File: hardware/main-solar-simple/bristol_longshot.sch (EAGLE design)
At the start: 65 parts, among them U1 SAM_D20E, U2 SI4060, U3 UBLOX_MAX, U4 SST25WF040BT-40I/NP, U5 TG-5006CJ, U6 LTC3105EDDPBF, U7 TPS3123, U8 SN74LVC1G32DCKR, U9 BMP180

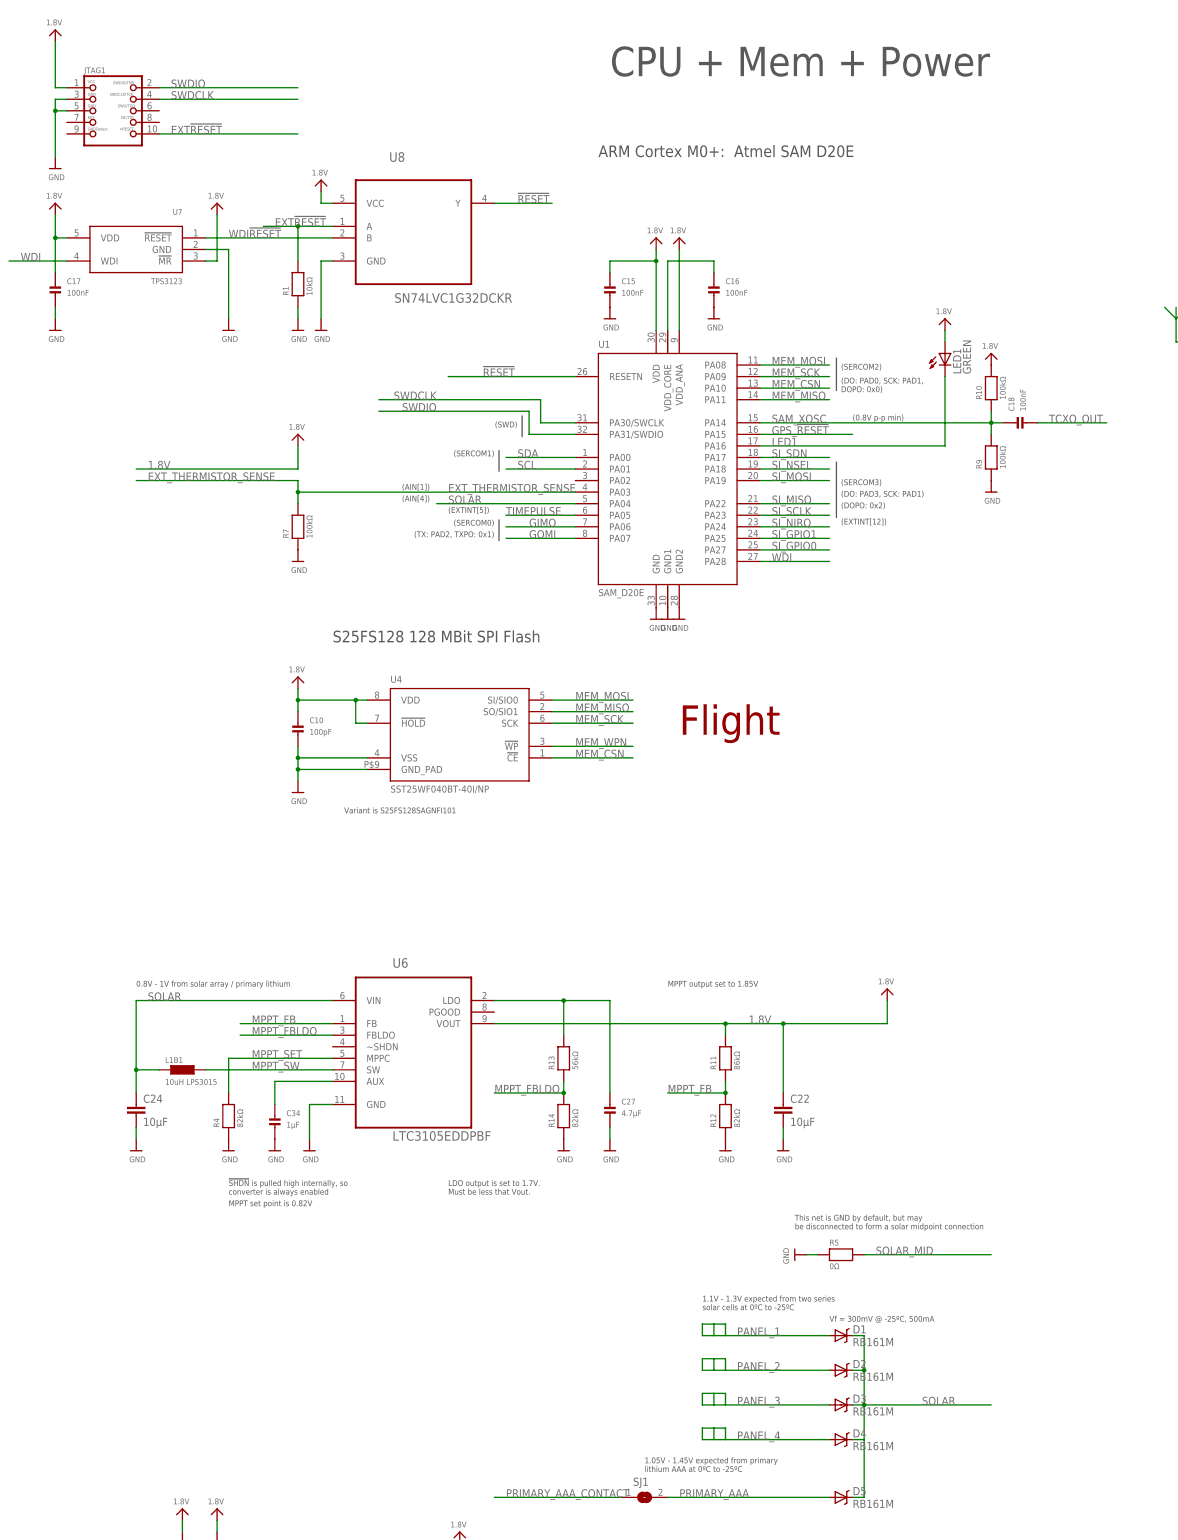
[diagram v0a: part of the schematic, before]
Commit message: Updated schematic labels, fixed R11 value
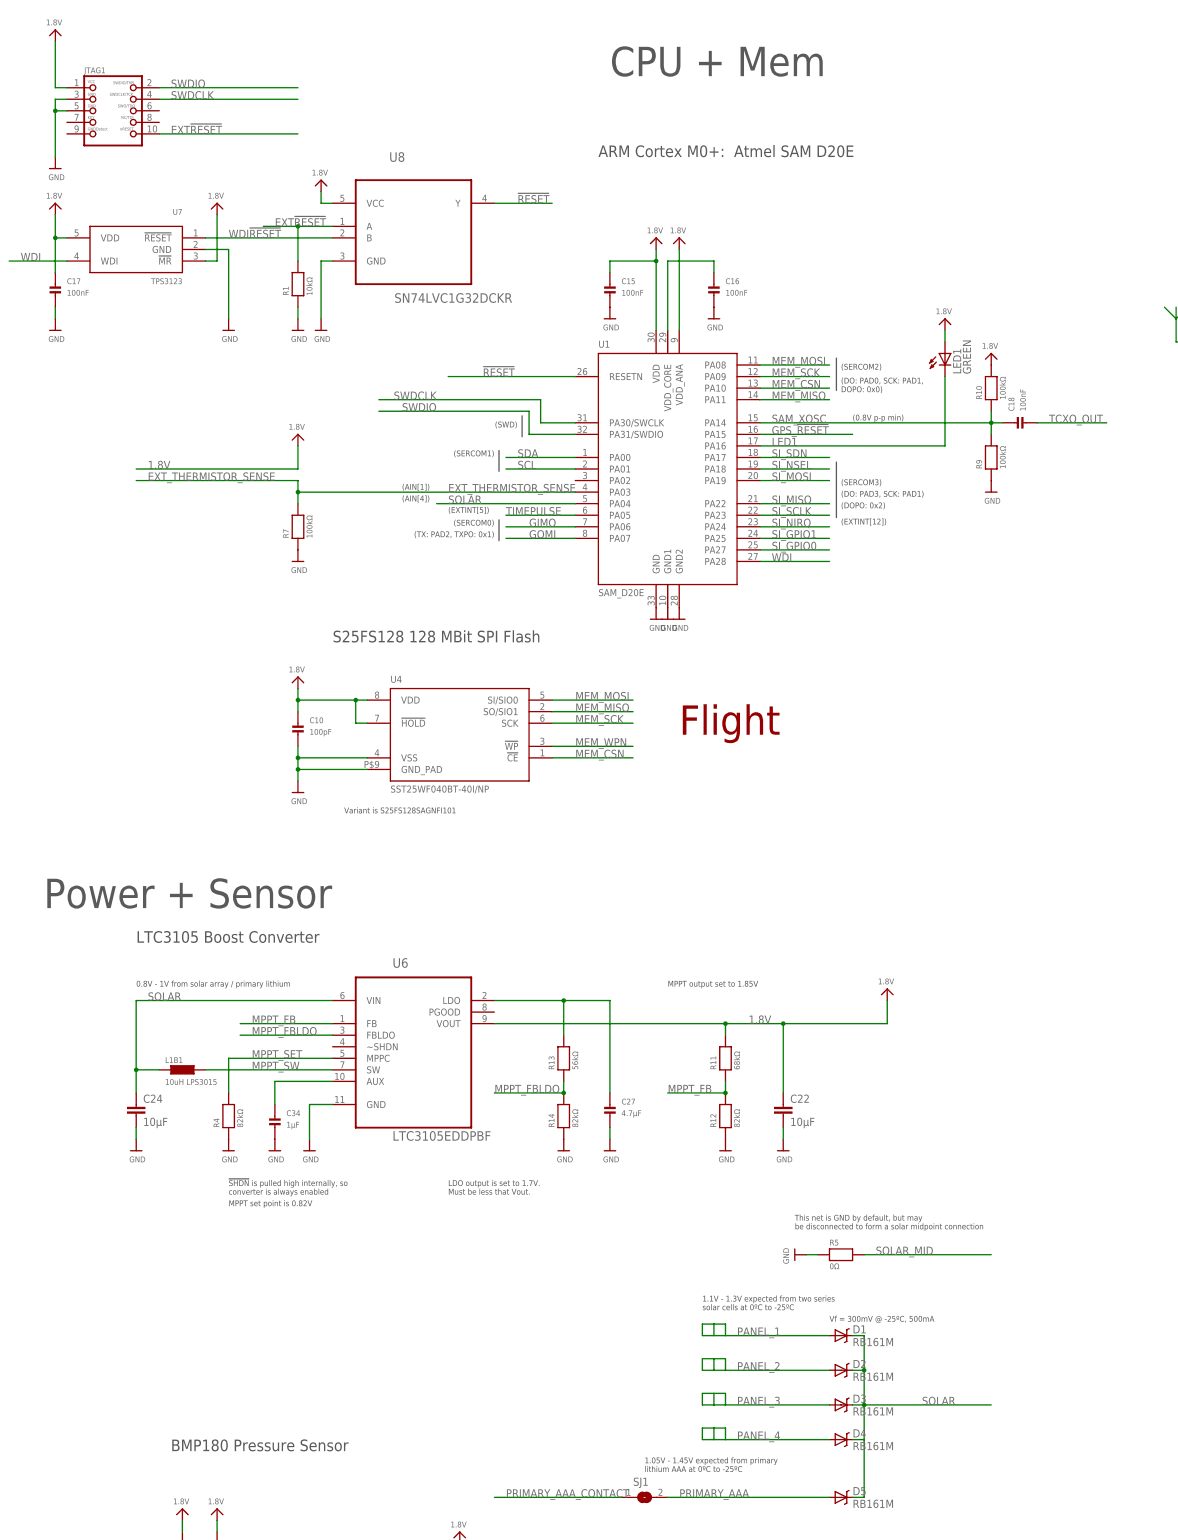
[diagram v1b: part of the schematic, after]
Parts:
- R11: value 86kΩ -> 68kΩ
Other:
- note added: "BMP180 Pressure Sensor"
- note added: "CPU + Mem"
- note added: "LTC3105 Boost Converter"
- note added: "Power + Sensor"
- note removed: "CPU + Mem + Power"
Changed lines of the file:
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@@
 <part name="FRAME4" library="SparkFun" deviceset="FRAME-LETTER" device=""/>
 <part name="R12" library="microbuilder_v3" deviceset="RESISTOR" device="_0402" value="82kΩ"/>
-<part name="R11" library="microbuilder_v3" deviceset="RESISTOR" device="_0402" value="86kΩ"/>
+<part name="R11" library="microbuilder_v3" deviceset="RESISTOR" device="_0402" value="68kΩ"/>
 <part name="U$33" library="microbuilder_v3" deviceset="GND" device=""/>
 <part name="C34" library="microbuilder_v3" deviceset="CAP_CERAMIC" device="_0402" value="1µF"/>
@@
 <text x="294.64" y="172.72" size="2.54" layer="97" font="vector" ratio="11">Si4060 Transmitter</text>
 <text x="269.24" y="119.888" size="1.27" layer="97" font="vector" ratio="11" distance="100">Tuned for 434MHz</text>
-<text x="134.62" y="170.18" size="6.4516" layer="97" font="vector" ratio="11">CPU + Mem + Power</text>
+<text x="134.62" y="170.18" size="6.4516" layer="97" font="vector" ratio="11">CPU + Mem</text>
 <text x="259.08" y="175.26" size="6.4516" layer="97" font="vector" ratio="11">Comms</text>
 <text x="403.86" y="25.4" size="6.4516" layer="94" font="vector" ratio="11">Flight</text>
@@
 <text x="175.26" y="-83.312" size="1.27" layer="97" font="vector" ratio="11">This net is GND by default, but may
 be disconnected to form a solar midpoint connection</text>
+<text x="30.48" y="-20.32" size="2.54" layer="97" font="vector" ratio="11">LTC3105 Boost Converter</text>
+<text x="38.1" y="-132.08" size="2.54" layer="97" font="vector" ratio="11">BMP180 Pressure Sensor</text>
+<text x="10.16" y="-12.7" size="6.4516" layer="97" font="vector" ratio="11">Power + Sensor</text>
 </plain>
 <instances>

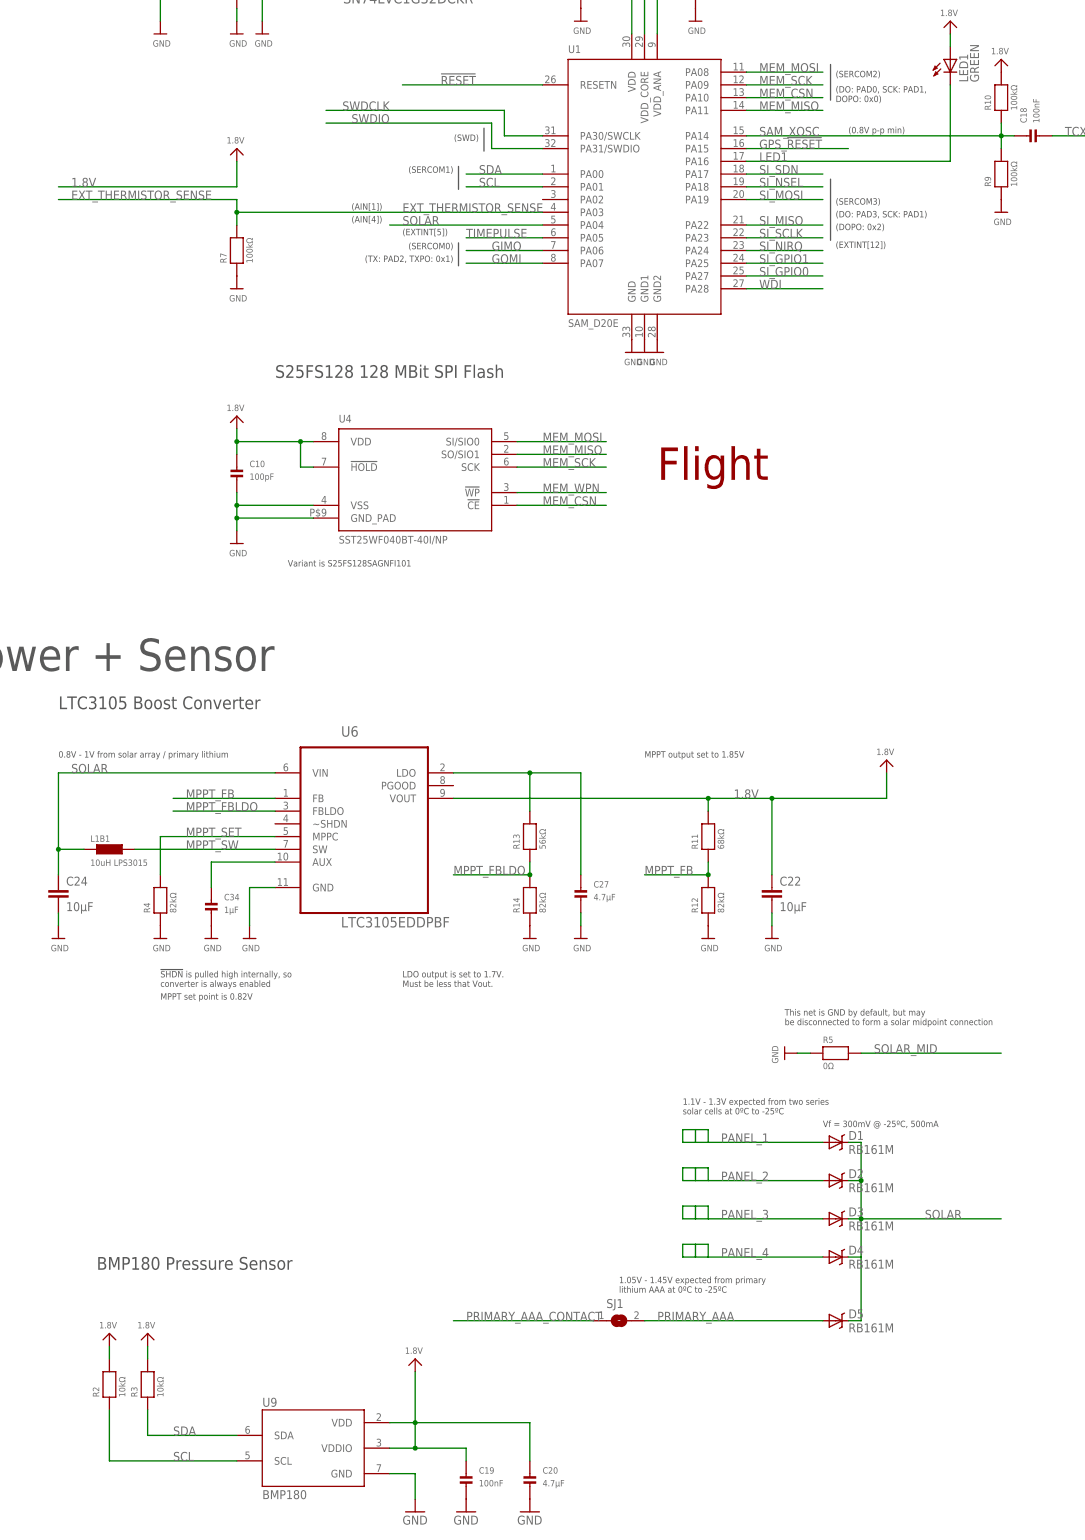
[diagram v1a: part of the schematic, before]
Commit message: Parts list complete for main-solar-simple (v0.985)
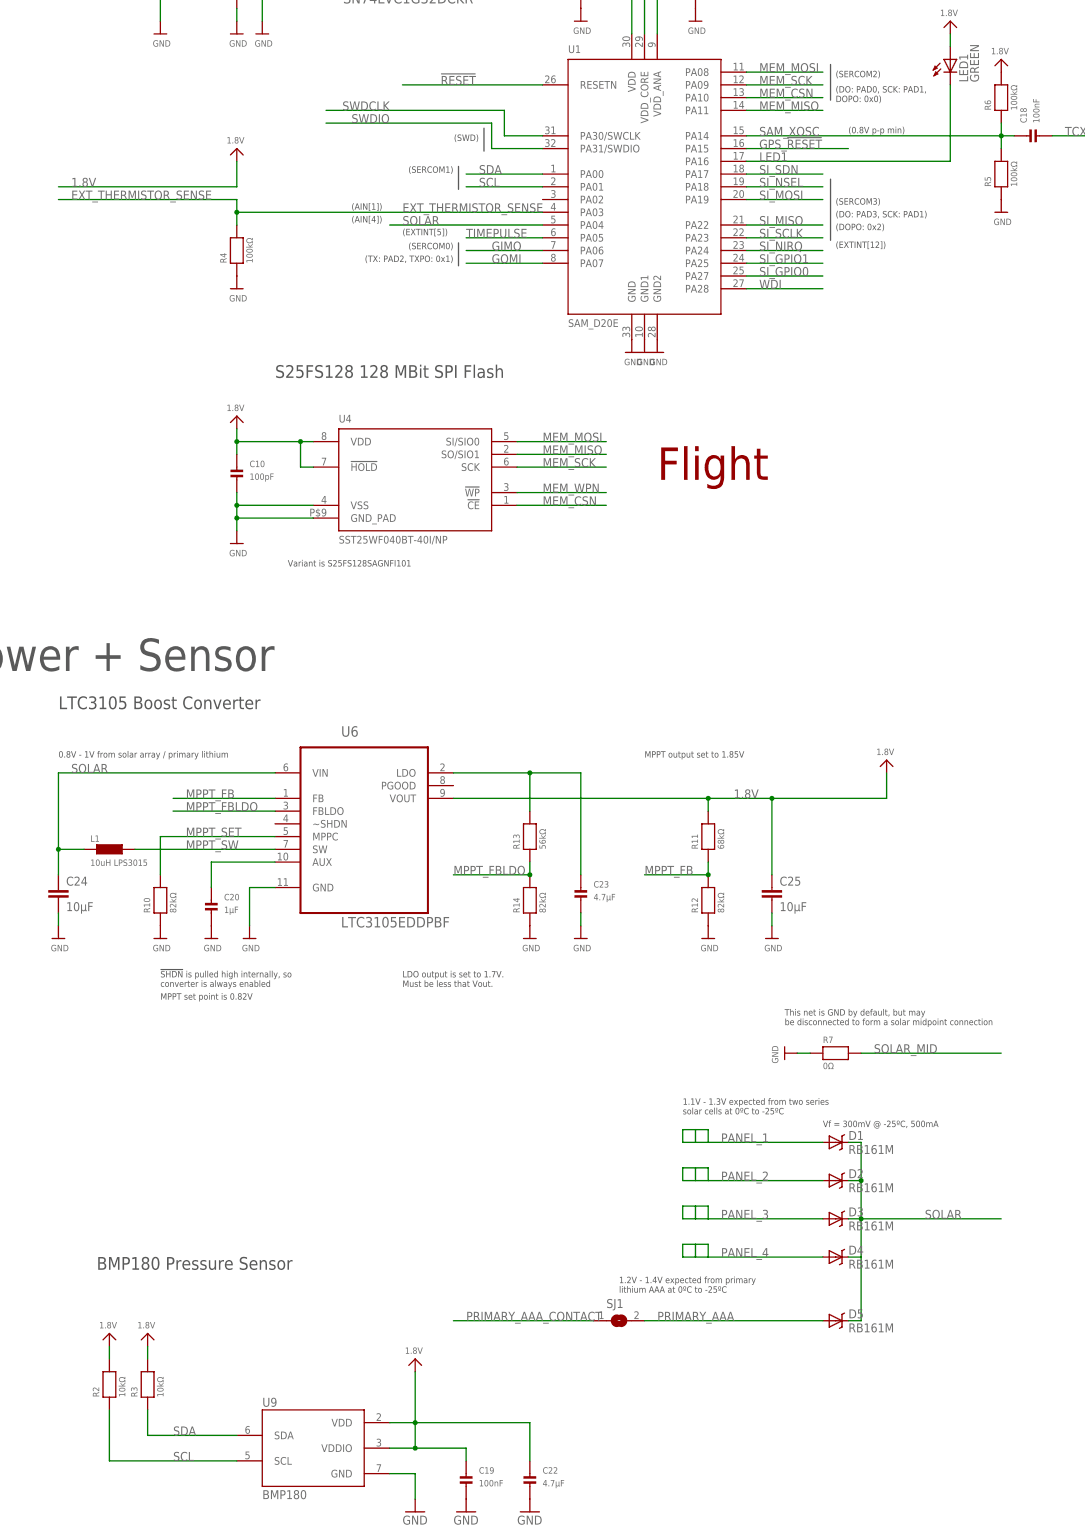
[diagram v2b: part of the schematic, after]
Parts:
- removed C34: 1µF, microbuilder_v3:CAP_CERAMIC_0402
- removed R9: 100kΩ, microbuilder_v3:RESISTOR_0402
- added C25: 10µF, resistor:C-EUC0603K
- added R6: 100kΩ, microbuilder_v3:RESISTOR_0402
- C20: value 4.7µF -> 1µF
- C22: value 10µF -> 4.7µF; device resistor:C-EUC0603K -> microbuilder_v3:CAP_CERAMIC_0402
- R10: value 100kΩ -> 82kΩ
- R4: value 82kΩ -> 100kΩ
- R5: value 0Ω -> 100kΩ
- R7: value 100kΩ -> 0Ω
- renumbered C27 to C23, L1B1 to L1
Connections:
- net 1.8V: now also C22.P$1, C25.1, R6.2; no longer C20.P$1, C22.1, R10.2
- net EXT_THERMISTOR_SENSE: now also R4.2; no longer R7.2
- net GND: now also C22.P$2, C25.2, R10.1; no longer C22.2, C34.P$2, R9.1
- net MPPT_AUX: now also C20.P$1; no longer C34.P$1
- net MPPT_SET: now also R10.2; no longer R4.2
- net SAM_XOSC: now also R5.2, R6.1; no longer R10.1, R9.2
- net SOLAR_MID: now also R7.2; no longer R5.2
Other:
- note added: "1.2V - 1.4V expected from primary lithium AAA at 0ºC to -25ºC"
- note removed: "1.05V - 1.45V expected from primary lithium AAA at 0ºC to -25ºC"
- moved on the sheet: C20, C22, R10, R4, R5, R7

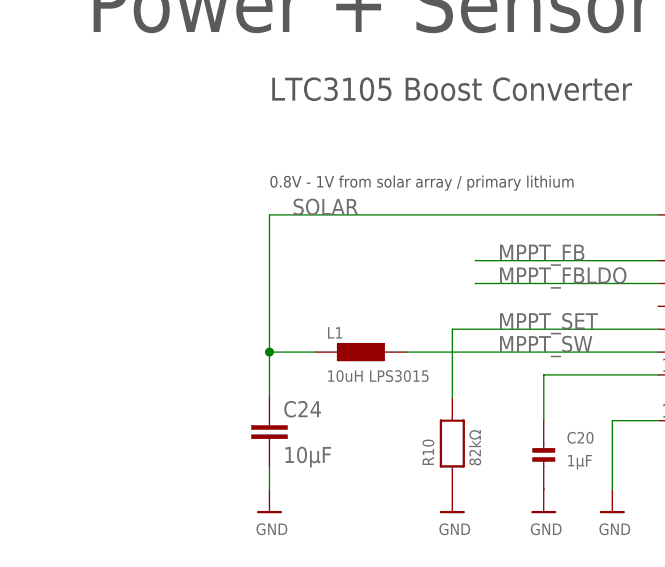
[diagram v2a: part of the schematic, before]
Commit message: Added DNP/0Ω for when using battery only on main-solar-simple
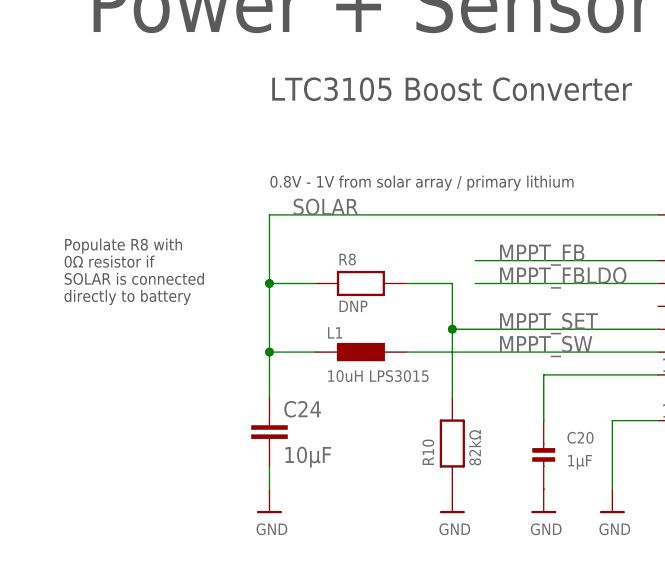
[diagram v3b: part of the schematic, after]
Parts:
- added R8: DNP, microbuilder_v3:RESISTOR_0402
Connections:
- net MPPT_SET: now also R8.2
- net SOLAR: now also R8.1
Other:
- note added: "Populate R8 with 0Ω resistor if SOLAR is connected directly to battery"
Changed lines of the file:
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@@
 <part name="R7" library="microbuilder_v3" deviceset="RESISTOR" device="_0402" value="0Ω"/>
 <part name="U$52" library="microbuilder_v3" deviceset="GND" device=""/>
+<part name="R8" library="microbuilder_v3" deviceset="RESISTOR" device="_0402" value="DNP"/>
 </parts>
 <sheets>
@@
 <text x="38.1" y="-132.08" size="2.54" layer="97" font="vector" ratio="11">BMP180 Pressure Sensor</text>
 <text x="10.16" y="-12.7" size="6.4516" layer="97" font="vector" ratio="11">Power + Sensor</text>
+<text x="7.62" y="-42.672" size="1.27" layer="97" font="vector" ratio="11">Populate R8 with
+0Ω resistor if
+SOLAR is connected
+directly to battery</text>
 </plain>
 <instances>
@@
 <instance part="R7" gate="G$1" x="185.42" y="-88.9"/>
 <instance part="U$52" gate="G$1" x="175.26" y="-88.9" rot="R270"/>
+<instance part="R8" gate="G$1" x="40.64" y="-40.64"/>
 </instances>
 <busses>
@@
 <pinref part="C24" gate="G$1" pin="1"/>
 <wire x1="73.66" y1="-33.02" x2="30.48" y2="-33.02" width="0.1524" layer="91"/>
-<wire x1="30.48" y1="-33.02" x2="30.48" y2="-48.26" width="0.1524" layer="91"/>
+<wire x1="30.48" y1="-33.02" x2="30.48" y2="-40.64" width="0.1524" layer="91"/>
 <pinref part="L1" gate="G$1" pin="1"/>
+<wire x1="30.48" y1="-40.64" x2="30.48" y2="-48.26" width="0.1524" layer="91"/>
 <wire x1="30.48" y1="-48.26" x2="30.48" y2="-53.34" width="0.1524" layer="91"/>
 <wire x1="35.56" y1="-48.26" x2="30.48" y2="-48.26" width="0.1524" layer="91"/>
 <junction x="30.48" y="-48.26"/>
 <label x="33.02" y="-33.02" size="1.778" layer="95"/>
+<pinref part="R8" gate="G$1" pin="1"/>
+<wire x1="35.56" y1="-40.64" x2="30.48" y2="-40.64" width="0.1524" layer="91"/>
+<junction x="30.48" y="-40.64"/>
 </segment>
 <segment>
@@
 <wire x1="50.8" y1="-45.72" x2="50.8" y2="-53.34" width="0.1524" layer="91"/>
 <label x="55.88" y="-45.72" size="1.778" layer="95"/>
-</segment>
-</net>
+<pinref part="R8" gate="G$1" pin="2"/>
+<wire x1="45.72" y1="-40.64" x2="50.8" y2="-40.64" width="0.1524" layer="91"/>
+<wire x1="50.8" y1="-40.64" x2="50.8" y2="-45.72" width="0.1524" layer="91"/>
+<junction x="50.8" y="-45.72"/>
+</segment>
+</net>
